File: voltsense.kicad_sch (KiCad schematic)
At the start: 9 parts, among them J32 POT

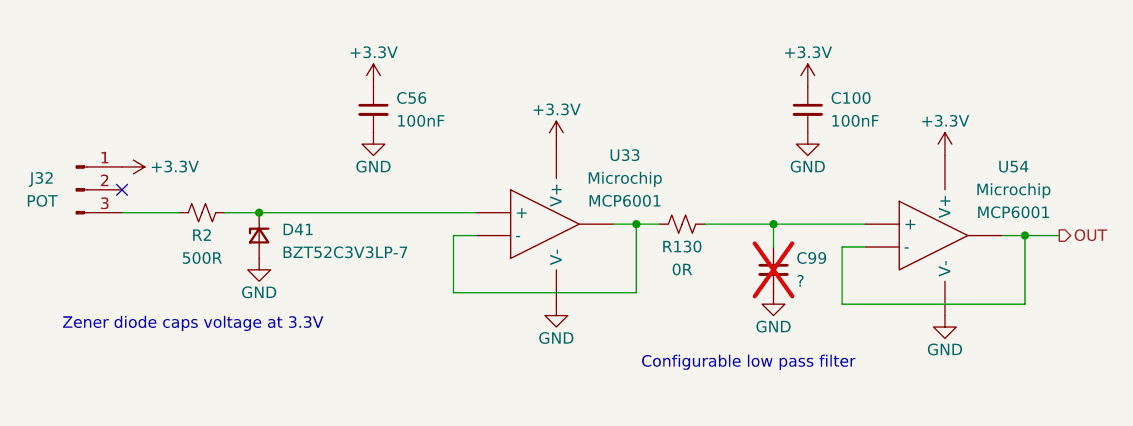
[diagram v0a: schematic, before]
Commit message: Updated to add beginnings of layout. Most major subsystems internally layed out
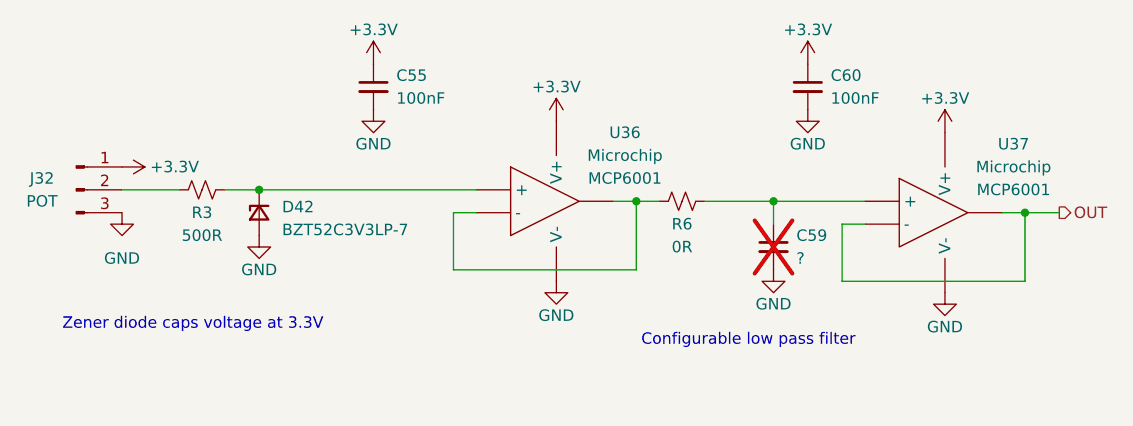
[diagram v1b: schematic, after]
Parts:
- removed C100, C56: 100nF, Capacitor_SMD:C_0402_1005Metric, symbol Device:C_Small
- removed C99: ?, Capacitor_SMD:C_0402_1005Metric, symbol Device:C_Small
- removed D41: BZT52C3V3LP-7, Diode_SMD:D_0402_1005Metric_Pad0.77x0.64mm_HandSolder, symbol UCIRP-KiCAD-Lib:D_Zener_Small
- removed R130: 0R, Resistor_SMD:R_0402_1005Metric, symbol Device:R_Small_US
- removed R2: 500R, Resistor_SMD:R_0402_1005Metric, symbol Device:R_Small_US
- removed U33, U54: ~, Package_TO_SOT_SMD:SOT-23-5, symbol UCIRP-KiCAD-Lib:MCP6001
- added C55, C60: 100nF, Capacitor_SMD:C_0402_1005Metric, symbol Device:C_Small
- added C59: ?, Capacitor_SMD:C_0402_1005Metric, symbol Device:C_Small
- added D42: BZT52C3V3LP-7, Diode_SMD:D_0402_1005Metric_Pad0.77x0.64mm_HandSolder, symbol UCIRP-KiCAD-Lib:D_Zener_Small
- added R3: 500R, Resistor_SMD:R_0402_1005Metric, symbol Device:R_Small_US
- added R6: 0R, Resistor_SMD:R_0402_1005Metric, symbol Device:R_Small_US
- added U36, U37: ~, Package_TO_SOT_SMD:SOT-23-5, symbol UCIRP-KiCAD-Lib:MCP6001
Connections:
- net +3.3V: now also C55.1, C60.1, U36.5 (V+), U37.5 (V+)
- net GND: now also J32.3 (Pin_3), C55.2, C59.2, C60.2, D42.2 (A), U36.2 (V-), U37.2 (V-)
- net OUT: now also U37.1, U37.4 (-)
- net at J32.2 (Pin_2): now also R3.2
- new net: C59.1, R6.1, U37.3 (+)
- new net: R6.2, U36.1, U36.4 (-)
- new net: D42.1 (K), R3.1, U36.3 (+)
- no-connect marks 1 -> 0

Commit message: Updated to add new filtering circuit
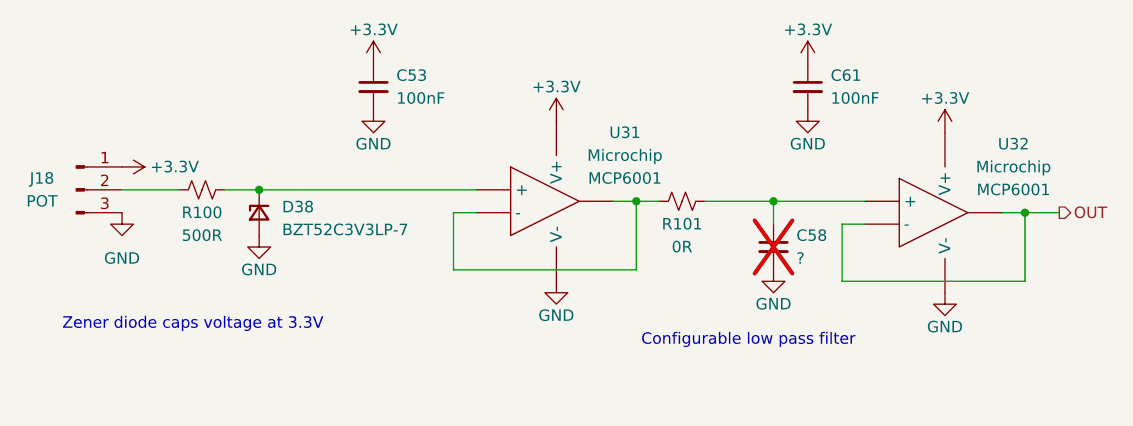
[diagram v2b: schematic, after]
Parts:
- renumbered C55 to C53, C59 to C58, C60 to C61, D42 to D38, J32 to J18, R3 to R100, R6 to R101, U36 to U31, U37 to U32
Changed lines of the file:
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@@
 		(on_board yes)
 		(dnp no)
-		(property "Reference" "#PWR058"
+		(property "Reference" "#PWR0179"
 			(at 97.79 111.76 0)
 			(effects
@@
 					(unit 1)
 				)
+				(path "/1eb2a3ff-e0fd-4343-8dba-716780a4d459/49c9c6d1-c766-4a15-8c23-ec8c2cd74e9d"
+					(reference "#PWR0179")
+					(unit 1)
+				)
 				(path "/1eb2a3ff-e0fd-4343-8dba-716780a4d459/65708f58-f753-44fb-8269-02151455b286"
 					(reference "#PWR0444")
@@
 		(on_board yes)
 		(dnp no)
-		(property "Reference" "J32"
+		(property "Reference" "J18"
 			(at 73.66 99.06 0)
 			(effects
@@
 					(unit 1)
 				)
+				(path "/1eb2a3ff-e0fd-4343-8dba-716780a4d459/49c9c6d1-c766-4a15-8c23-ec8c2cd74e9d"
+					(reference "J18")
+					(unit 1)
+				)
 				(path "/1eb2a3ff-e0fd-4343-8dba-716780a4d459/65708f58-f753-44fb-8269-02151455b286"
 					(reference "J37")
@@
 		(on_board yes)
 		(dnp no)
-		(property "Reference" "C55"
+		(property "Reference" "C53"
 			(at 113.03 87.63 0)
 			(effects
@@
 					(unit 1)
 				)
+				(path "/1eb2a3ff-e0fd-4343-8dba-716780a4d459/49c9c6d1-c766-4a15-8c23-ec8c2cd74e9d"
+					(reference "C53")
+					(unit 1)
+				)
 				(path "/1eb2a3ff-e0fd-4343-8dba-716780a4d459/65708f58-f753-44fb-8269-02151455b286"
 					(reference "C104")
@@
 		(on_board yes)
 		(dnp no)
-		(property "Reference" "R6"
+		(property "Reference" "R101"
 			(at 144.78 104.14 90)
 			(effects
@@
 					(unit 1)
 				)
+				(path "/1eb2a3ff-e0fd-4343-8dba-716780a4d459/49c9c6d1-c766-4a15-8c23-ec8c2cd74e9d"
+					(reference "R101")
+					(unit 1)
+				)
 				(path "/1eb2a3ff-e0fd-4343-8dba-716780a4d459/65708f58-f753-44fb-8269-02151455b286"
 					(reference "R133")
@@
 		(on_board yes)
 		(dnp no)
-		(property "Reference" "#PWR0430"
+		(property "Reference" "#PWR0189"
 			(at 158.75 90.17 0)
 			(effects
@@
 					(unit 1)
 				)
+				(path "/1eb2a3ff-e0fd-4343-8dba-716780a4d459/49c9c6d1-c766-4a15-8c23-ec8c2cd74e9d"
+					(reference "#PWR0189")
+					(unit 1)
+				)
 				(path "/1eb2a3ff-e0fd-4343-8dba-716780a4d459/65708f58-f753-44fb-8269-02151455b286"
 					(reference "#PWR0450")
@@
 		(on_board yes)
 		(dnp yes)
-		(property "Reference" "C59"
+		(property "Reference" "C58"
 			(at 157.48 105.41 0)
 			(effects
@@
 					(unit 1)
 				)
+				(path "/1eb2a3ff-e0fd-4343-8dba-716780a4d459/49c9c6d1-c766-4a15-8c23-ec8c2cd74e9d"
+					(reference "C58")
+					(unit 1)
+				)
 				(path "/1eb2a3ff-e0fd-4343-8dba-716780a4d459/65708f58-f753-44fb-8269-02151455b286"
 					(reference "C105")
@@
 		(on_board yes)
 		(dnp no)
-		(property "Reference" "#PWR073"
+		(property "Reference" "#PWR0184"
 			(at 130.81 96.52 0)
 			(effects
@@
 					(unit 1)
 				)
+				(path "/1eb2a3ff-e0fd-4343-8dba-716780a4d459/49c9c6d1-c766-4a15-8c23-ec8c2cd74e9d"
+					(reference "#PWR0184")
+					(unit 1)
+				)
 				(path "/1eb2a3ff-e0fd-4343-8dba-716780a4d459/65708f58-f753-44fb-8269-02151455b286"
 					(reference "#PWR0447")
@@
 		(on_board yes)
 		(dnp no)
-		(property "Reference" "#PWR0432"
+		(property "Reference" "#PWR0191"
 			(at 173.99 97.79 0)
 			(effects
@@
 				(path "/1eb2a3ff-e0fd-4343-8dba-716780a4d459/3ee7605e-1827-49f4-9069-e6dc2d01bdcd"
 					(reference "#PWR0442")
+					(unit 1)
+				)
+				(path "/1eb2a3ff-e0fd-4343-8dba-716780a4d459/49c9c6d1-c766-4a15-8c23-ec8c2cd74e9d"
+					(reference "#PWR0191")
 					(unit 1)
 				)
@@
 		(dnp no)
 		(fields_autoplaced yes)
-		(property "Reference" "#PWR027"
+		(property "Reference" "#PWR0178"
 			(at 82.55 109.22 0)
 			(effects
@@
 				)
 				(path "/1eb2a3ff-e0fd-4343-8dba-716780a4d459/243e7ef2-3d1b-47c4-9f99-7492be586247"
-					(reference "#PWR027")
-					(unit 1)
-				)
-				(path "/1eb2a3ff-e0fd-4343-8dba-716780a4d459/3ee7605e-1827-49f4-9069-e6dc2d01bdcd"
-					(reference "#PWR028")
-					(unit 1)
-				)
-				(path "/1eb2a3ff-e0fd-4343-8dba-716780a4d459/65708f58-f753-44fb-8269-02151455b286"
-					(reference "#PWR038")
+					(reference "#PWR039")
+					(unit 1)
+				)
+				(path "/1eb2a3ff-e0fd-4343-8dba-716780a4d459/3ee7605e-1827-49f4-9069-e6dc2d01bdcd"
+					(reference "#PWR039")
+					(unit 1)
+				)
+				(path "/1eb2a3ff-e0fd-4343-8dba-716780a4d459/49c9c6d1-c766-4a15-8c23-ec8c2cd74e9d"
+					(reference "#PWR0178")
+					(unit 1)
+				)
+				(path "/1eb2a3ff-e0fd-4343-8dba-716780a4d459/65708f58-f753-44fb-8269-02151455b286"
+					(reference "#PWR039")
 					(unit 1)
 				)
@@
 		(on_board yes)
 		(dnp no)
-		(property "Reference" "R3"
+		(property "Reference" "R100"
 			(at 91.44 102.87 90)
 			(effects
@@
 					(unit 1)
 				)
+				(path "/1eb2a3ff-e0fd-4343-8dba-716780a4d459/49c9c6d1-c766-4a15-8c23-ec8c2cd74e9d"
+					(reference "R100")
+					(unit 1)
+				)
 				(path "/1eb2a3ff-e0fd-4343-8dba-716780a4d459/65708f58-f753-44fb-8269-02151455b286"
 					(reference "R132")
@@
 		(on_board yes)
 		(dnp no)
-		(property "Reference" "#PWR0431"
+		(property "Reference" "#PWR0190"
 			(at 158.75 97.79 0)
 			(effects
@@
 				(path "/1eb2a3ff-e0fd-4343-8dba-716780a4d459/3ee7605e-1827-49f4-9069-e6dc2d01bdcd"
 					(reference "#PWR0441")
+					(unit 1)
+				)
+				(path "/1eb2a3ff-e0fd-4343-8dba-716780a4d459/49c9c6d1-c766-4a15-8c23-ec8c2cd74e9d"
+					(reference "#PWR0190")
 					(unit 1)
 				)
@@
 		(dnp no)
 		(fields_autoplaced yes)
-		(property "Reference" "D42"
+		(property "Reference" "D38"
 			(at 100.33 102.235 90)
 			(effects
@@
 					(unit 1)
 				)
+				(path "/1eb2a3ff-e0fd-4343-8dba-716780a4d459/49c9c6d1-c766-4a15-8c23-ec8c2cd74e9d"
+					(reference "D38")
+					(unit 1)
+				)
 				(path "/1eb2a3ff-e0fd-4343-8dba-716780a4d459/65708f58-f753-44fb-8269-02151455b286"
 					(reference "D44")
@@
 		(on_board yes)
 		(dnp no)
-		(property "Reference" "#PWR072"
+		(property "Reference" "#PWR0183"
 			(at 110.49 97.79 0)
 			(effects
@@
 					(unit 1)
 				)
+				(path "/1eb2a3ff-e0fd-4343-8dba-716780a4d459/49c9c6d1-c766-4a15-8c23-ec8c2cd74e9d"
+					(reference "#PWR0183")
+					(unit 1)
+				)
 				(path "/1eb2a3ff-e0fd-4343-8dba-716780a4d459/65708f58-f753-44fb-8269-02151455b286"
 					(reference "#PWR0446")
@@
 		(on_board yes)
 		(dnp no)
-		(property "Reference" "U36"
+		(property "Reference" "U31"
 			(at 138.43 93.98 0)
 			(effects
@@
 					(unit 1)
 				)
+				(path "/1eb2a3ff-e0fd-4343-8dba-716780a4d459/49c9c6d1-c766-4a15-8c23-ec8c2cd74e9d"
+					(reference "U31")
+					(unit 1)
+				)
 				(path "/1eb2a3ff-e0fd-4343-8dba-716780a4d459/65708f58-f753-44fb-8269-02151455b286"
 					(reference "U56")
@@
 		(on_board yes)
 		(dnp no)
-		(property "Reference" "#PWR092"
+		(property "Reference" "#PWR0185"
 			(at 130.81 116.84 0)
 			(effects
@@
 					(unit 1)
 				)
+				(path "/1eb2a3ff-e0fd-4343-8dba-716780a4d459/49c9c6d1-c766-4a15-8c23-ec8c2cd74e9d"
+					(reference "#PWR0185")
+					(unit 1)
+				)
 				(path "/1eb2a3ff-e0fd-4343-8dba-716780a4d459/65708f58-f753-44fb-8269-02151455b286"
 					(reference "#PWR0448")
@@
 		(on_board yes)
 		(dnp no)
-		(property "Reference" "C60"
+		(property "Reference" "C61"
 			(at 161.29 87.63 0)
 			(effects
@@
 					(unit 1)
 				)
+				(path "/1eb2a3ff-e0fd-4343-8dba-716780a4d459/49c9c6d1-c766-4a15-8c23-ec8c2cd74e9d"
+					(reference "C61")
+					(unit 1)
+				)
 				(path "/1eb2a3ff-e0fd-4343-8dba-716780a4d459/65708f58-f753-44fb-8269-02151455b286"
 					(reference "C106")
@@
 		(on_board yes)
 		(dnp no)
-		(property "Reference" "#PWR063"
+		(property "Reference" "#PWR0182"
 			(at 110.49 90.17 0)
 			(effects
@@
 					(unit 1)
 				)
+				(path "/1eb2a3ff-e0fd-4343-8dba-716780a4d459/49c9c6d1-c766-4a15-8c23-ec8c2cd74e9d"
+					(reference "#PWR0182")
+					(unit 1)
+				)
 				(path "/1eb2a3ff-e0fd-4343-8dba-716780a4d459/65708f58-f753-44fb-8269-02151455b286"
 					(reference "#PWR0445")
@@
 		(on_board yes)
 		(dnp no)
-		(property "Reference" "#PWR093"
+		(property "Reference" "#PWR0188"
 			(at 154.94 115.57 0)
 			(effects
@@
 					(unit 1)
 				)
+				(path "/1eb2a3ff-e0fd-4343-8dba-716780a4d459/49c9c6d1-c766-4a15-8c23-ec8c2cd74e9d"
+					(reference "#PWR0188")
+					(unit 1)
+				)
 				(path "/1eb2a3ff-e0fd-4343-8dba-716780a4d459/65708f58-f753-44fb-8269-02151455b286"
 					(reference "#PWR0449")
@@
 		(on_board yes)
 		(dnp no)
-		(property "Reference" "#PWR04"
+		(property "Reference" "#PWR0177"
 			(at 78.74 97.79 0)
 			(effects
@@
 					(unit 1)
 				)
+				(path "/1eb2a3ff-e0fd-4343-8dba-716780a4d459/49c9c6d1-c766-4a15-8c23-ec8c2cd74e9d"
+					(reference "#PWR0177")
+					(unit 1)
+				)
 				(path "/1eb2a3ff-e0fd-4343-8dba-716780a4d459/65708f58-f753-44fb-8269-02151455b286"
 					(reference "#PWR0408")
@@
 		(on_board yes)
 		(dnp no)
-		(property "Reference" "#PWR0433"
+		(property "Reference" "#PWR0194"
 			(at 173.99 118.11 0)
 			(effects
@@
 					(unit 1)
 				)
+				(path "/1eb2a3ff-e0fd-4343-8dba-716780a4d459/49c9c6d1-c766-4a15-8c23-ec8c2cd74e9d"
+					(reference "#PWR0194")
+					(unit 1)
+				)
 				(path "/1eb2a3ff-e0fd-4343-8dba-716780a4d459/65708f58-f753-44fb-8269-02151455b286"
 					(reference "#PWR0453")
@@
 		(on_board yes)
 		(dnp no)
-		(property "Reference" "U37"
+		(property "Reference" "U32"
 			(at 181.61 95.25 0)
 			(effects
@@
 					(unit 1)
 				)
+				(path "/1eb2a3ff-e0fd-4343-8dba-716780a4d459/49c9c6d1-c766-4a15-8c23-ec8c2cd74e9d"
+					(reference "U32")
+					(unit 1)
+				)

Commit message: Subsystem level layout done (prelim)
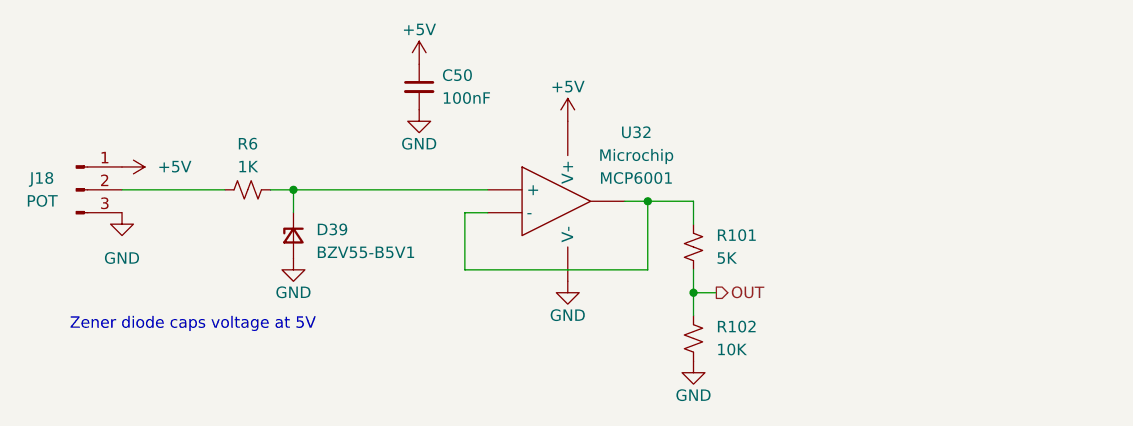
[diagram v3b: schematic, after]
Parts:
- removed C53, C61: 100nF, Capacitor_SMD:C_0402_1005Metric, symbol Device:C_Small
- removed C58: ?, Capacitor_SMD:C_0402_1005Metric, symbol Device:C_Small
- removed D38: BZT52C3V3LP-7, Diode_SMD:D_0402_1005Metric_Pad0.77x0.64mm_HandSolder, symbol UCIRP-KiCAD-Lib:D_Zener_Small
- removed R100: 500R, Resistor_SMD:R_0402_1005Metric, symbol Device:R_Small_US
- removed U31: ~, Package_TO_SOT_SMD:SOT-23-5, symbol UCIRP-KiCAD-Lib:MCP6001
- added C50: 100nF, Capacitor_SMD:C_0603_1608Metric, symbol Device:C_Small
- added D39: BZV55-B5V1, Diode_SMD:D_MiniMELF, symbol UCIRP-KiCAD-Lib:D_Zener_Small
- added R102: 10K, Resistor_SMD:R_0603_1608Metric, symbol Device:R_Small_US
- added R6: 1K, Resistor_SMD:R_0603_1608Metric, symbol Device:R_Small_US
- R101: value 0R -> 5K; footprint Resistor_SMD:R_0402_1005Metric -> Resistor_SMD:R_0603_1608Metric; Part # Generic 1K 1% 0402 Resistor -> Generic 5K 1% 0402 Resistor
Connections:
- net GND: now also C50.2, D39.2 (A), R102.1
- net OUT: now also R101.1, R102.2; no longer U32.1, U32.4 (-)
- net at J18.2 (Pin_2): now also R6.1
- net at U32.3 (+): now also D39.1 (K), R6.2; no longer R101.1
- net at R101.2: now also U32.1, U32.4 (-)
- net +3.3V renamed +5V
- net +5V: now also C50.1
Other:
- note added: "Zener diode caps voltage at 5V"
- note removed: "Configurable low pass filter"
- note removed: "Zener diode caps voltage at 3.3V"
